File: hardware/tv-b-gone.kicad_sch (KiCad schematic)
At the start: 0 parts

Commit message: Power lines added to KiCad schematic
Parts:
- added C1: 100n, symbol Device:C
- added U1: ATtiny85-20P, Package_DIP:DIP-8_W7.62mm, symbol MCU_Microchip_ATtiny:ATtiny85-20P
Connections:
- new net +5V: C1.2, U1.8 (VCC)
- new net GND: C1.1, U1.4 (GND)

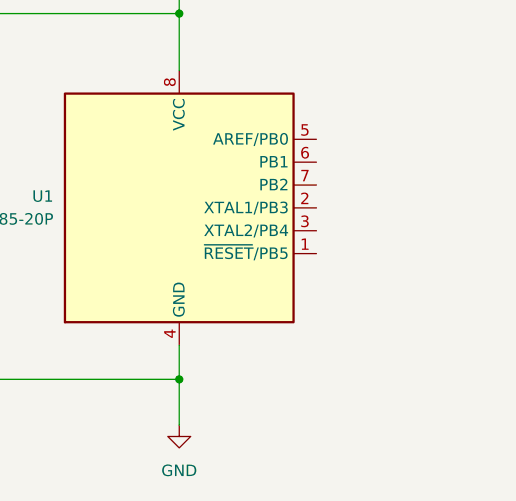
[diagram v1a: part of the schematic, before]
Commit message: added reset circuitry
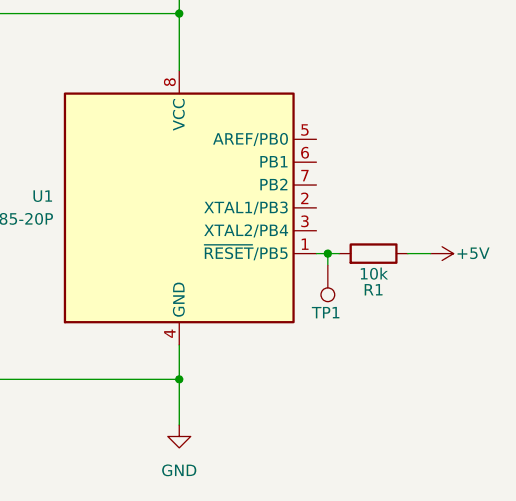
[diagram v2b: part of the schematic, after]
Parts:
- added R1: 10k, Resistor_SMD:R_0805_2012Metric, symbol Device:R
- added TP1: TestPoint, Connector:Tag-Connect_TC2030-IDC-FP_2x03_P1.27mm_Vertical, symbol Connector:TestPoint
- C1: footprint (none) -> Capacitor_SMD:C_0805_2012Metric
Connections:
- net +5V: now also R1.1
- net at U1.1 (~{RESET}/PB5): now also R1.2, TP1.1

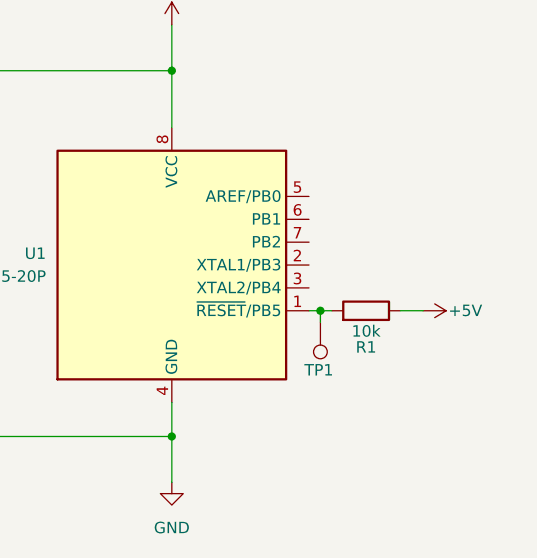
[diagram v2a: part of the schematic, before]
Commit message: ICSP test points added to schematic
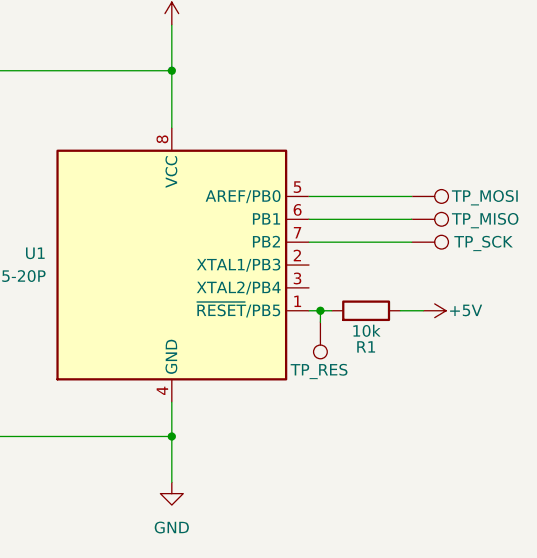
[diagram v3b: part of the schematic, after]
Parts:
- added TP_MISO, TP_MOSI, TP_SCK: TestPoint, TestPoint:TestPoint_Pad_D2.0mm, symbol Connector:TestPoint
- renumbered TP1 to TP_RES
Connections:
- net at U1.5 (AREF/PB0): now also TP_MOSI.1
- net at U1.6 (PB1): now also TP_MISO.1
- net at U1.7 (PB2): now also TP_SCK.1

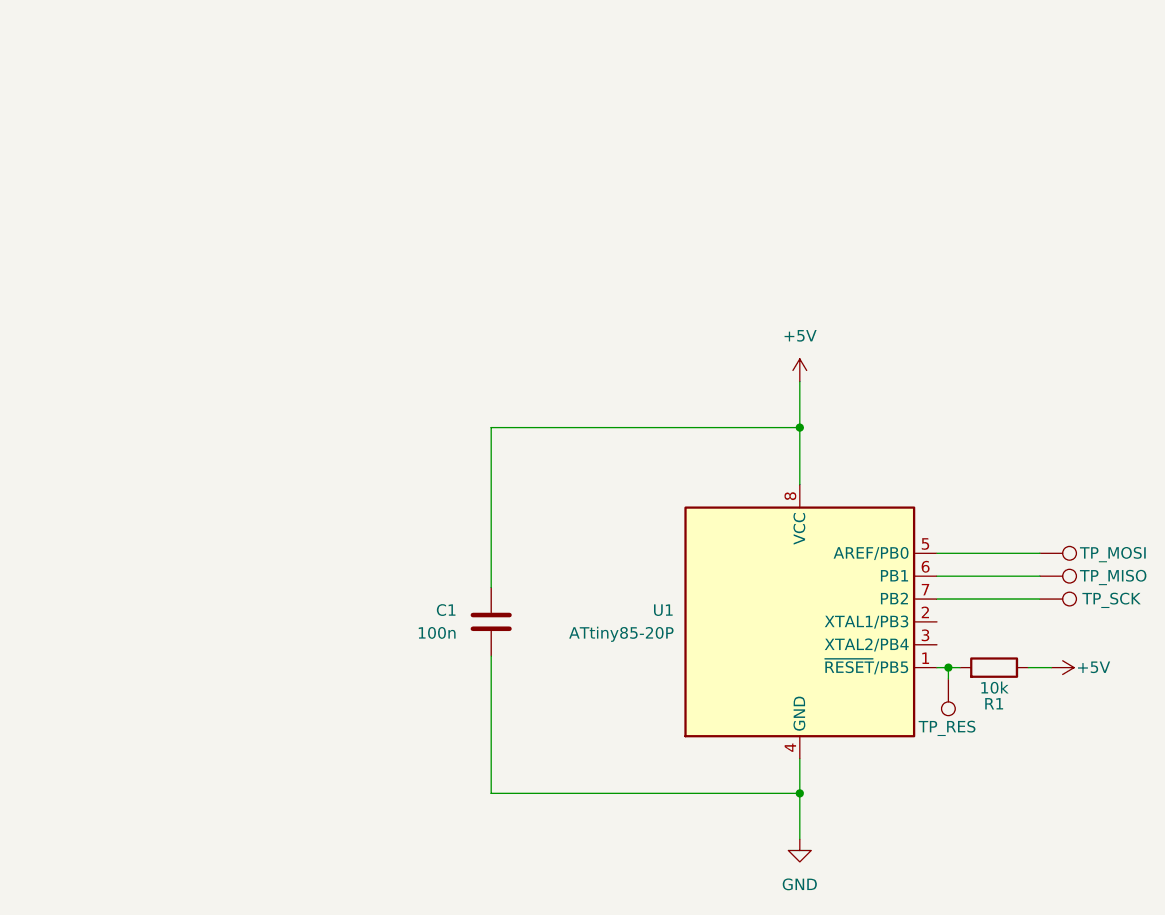
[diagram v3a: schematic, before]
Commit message: Added an IR LED and an N channel MOSFET for controlling it
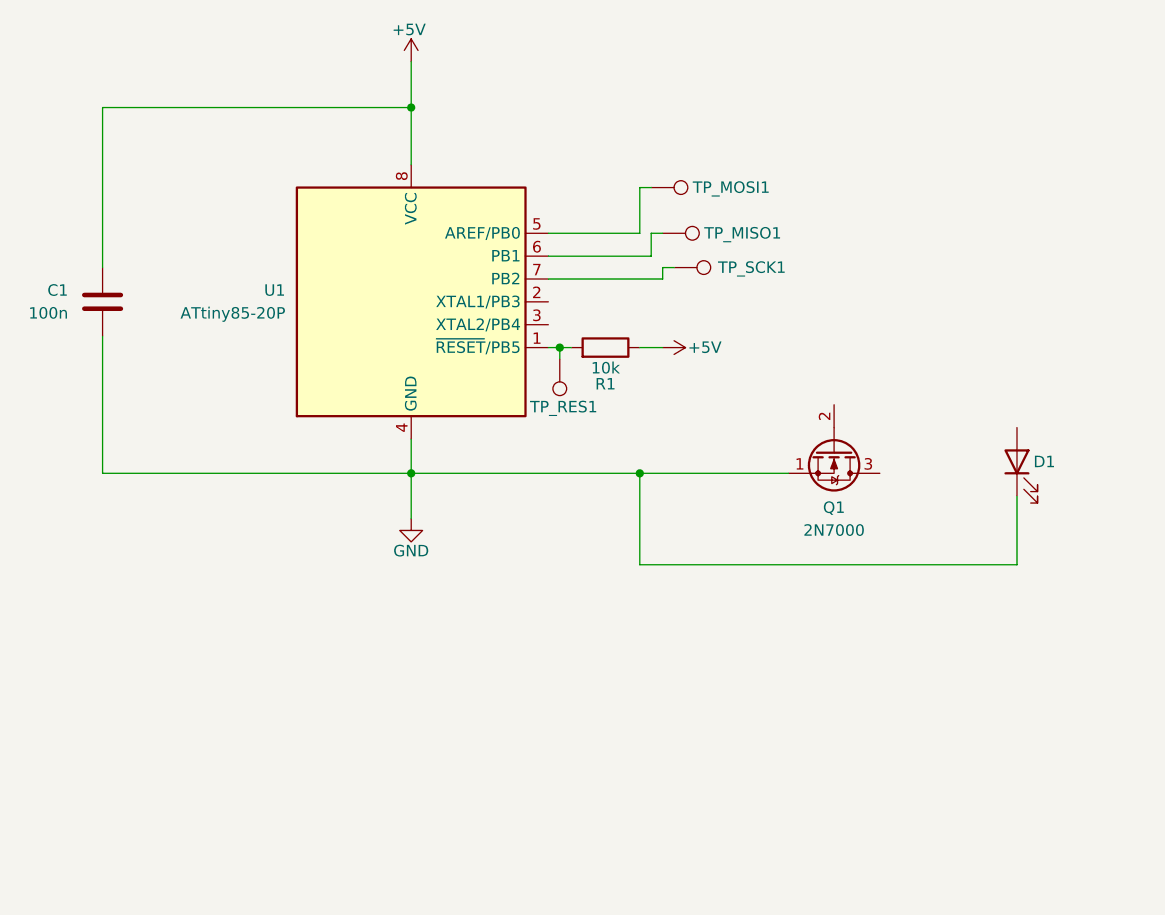
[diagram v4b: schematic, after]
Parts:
- added D1: LED, LED_THT:LED_D5.0mm, symbol Device:LED
- added Q1: 2N7000, Package_TO_SOT_THT:TO-92_Inline, symbol Transistor_FET:2N7000
- TP_RES1: renamed from TP_RES; footprint Connector:Tag-Connect_TC2030-IDC-FP_2x03_P1.27mm_Vertical -> TestPoint:TestPoint_Pad_D2.0mm
- renumbered TP_MISO to TP_MISO1, TP_MOSI to TP_MOSI1, TP_SCK to TP_SCK1
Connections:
- net GND: now also D1.1 (K), Q1.1 (S)
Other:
- title: (none) -> tv-b-gone main PCB
- moved on the sheet: C1, R1, TP_MISO1, TP_MOSI1, TP_RES1, TP_SCK1, U1

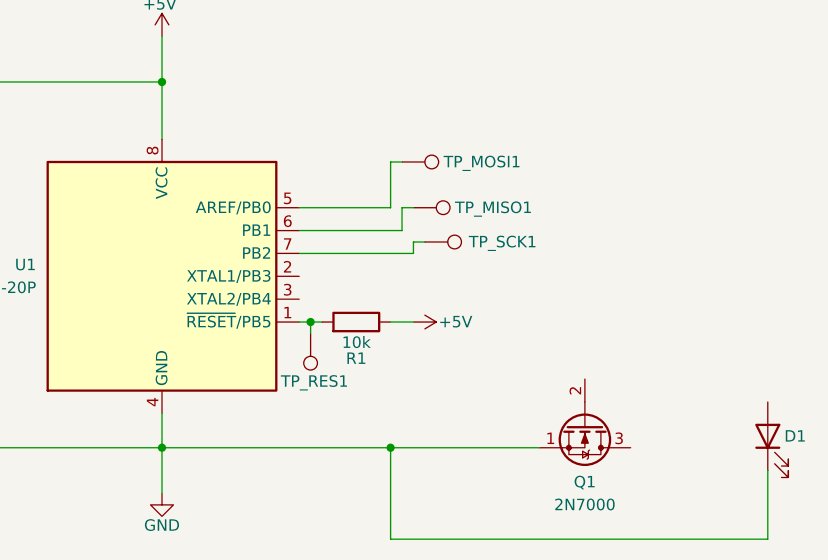
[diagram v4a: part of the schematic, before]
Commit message: Wired the mosfet to the IR LED
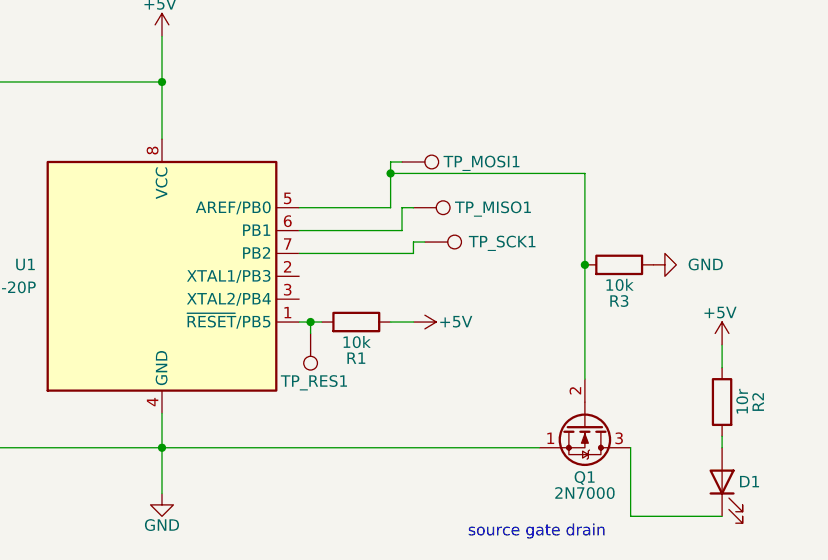
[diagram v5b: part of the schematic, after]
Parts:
- added R2: 10r, Resistor_SMD:R_0805_2012Metric, symbol Device:R
- added R3: 10k, Resistor_SMD:R_0805_2012Metric, symbol Device:R
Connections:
- net +5V: now also R2.1
- net GND: now also R3.1; no longer D1.1 (K)
- net at TP_MOSI1.1, U1.5 (AREF/PB0): now also Q1.2 (G), R3.2
- net at D1.2 (A): now also R2.2
- net at Q1.3 (D): now also D1.1 (K)
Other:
- note added: "source gate drain"
- moved on the sheet: D1

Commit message: Fixed references for ICSP connections
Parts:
- renumbered TP_MISO1 to TP_MISO, TP_MOSI1 to TP_MOSI, TP_RES1 to TP_RESET, TP_SCK1 to TP_SCK
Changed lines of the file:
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@@
 		(in_pos_files yes)
 		(dnp no)
-		(property "Reference" "TP_MOSI1"
+		(property "Reference" "TP_MOSI"
 			(at 114.808 49.53 90)
 			(show_name no)
@@
 			(project "tv-b-gone"
 				(path "/23a371e7-c0c2-4fe5-805f-b61be48edc46"
-					(reference "TP_MOSI1")
+					(reference "TP_MOSI")
 					(unit 1)
 				)
@@
 		(in_pos_files yes)
 		(dnp no)
-		(property "Reference" "TP_RES1"
+		(property "Reference" "TP_RESET"
 			(at 88.138 73.914 0)
 			(show_name no)
@@
 			(project "tv-b-gone"
 				(path "/23a371e7-c0c2-4fe5-805f-b61be48edc46"
-					(reference "TP_RES1")
+					(reference "TP_RESET")
 					(unit 1)
 				)
@@
 		(in_pos_files yes)
 		(dnp no)
-		(property "Reference" "TP_SCK1"
+		(property "Reference" "TP_SCK"
 			(at 116.586 58.42 90)
 			(show_name no)
@@
 			(project "tv-b-gone"
 				(path "/23a371e7-c0c2-4fe5-805f-b61be48edc46"
-					(reference "TP_SCK1")
+					(reference "TP_SCK")
 					(unit 1)
 				)
@@
 		(in_pos_files yes)
 		(dnp no)
-		(property "Reference" "TP_MISO1"
+		(property "Reference" "TP_MISO"
 			(at 116.078 54.61 90)
 			(show_name no)
@@
 			(project "tv-b-gone"
 				(path "/23a371e7-c0c2-4fe5-805f-b61be48edc46"
-					(reference "TP_MISO1")
-					(unit 1)
-				)
+					(reference "TP_MISO")
+					(unit 1)
+				)

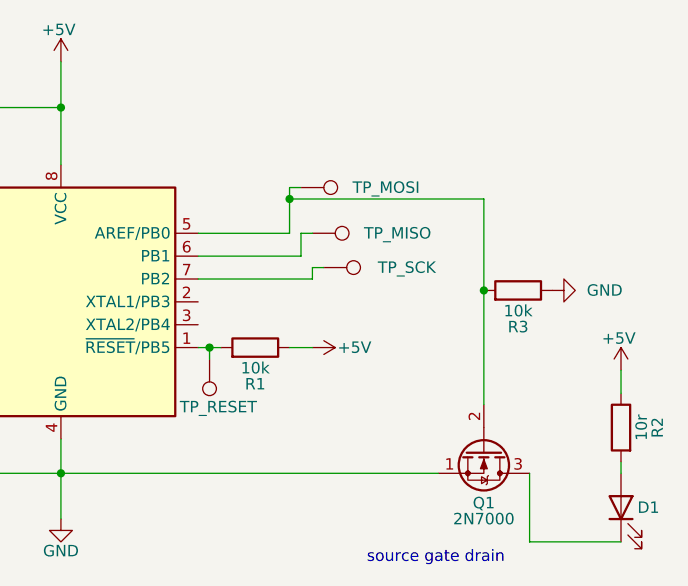
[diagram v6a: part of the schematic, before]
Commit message: Added a tactile switch
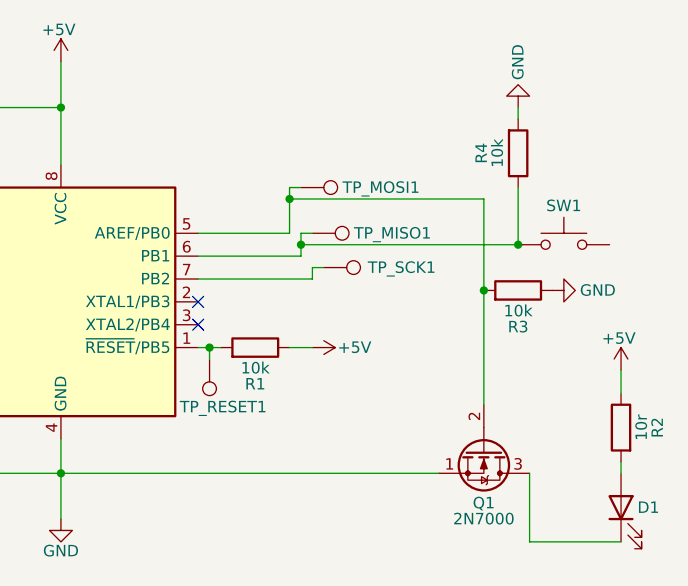
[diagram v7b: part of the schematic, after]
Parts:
- added R4: 10k, Resistor_SMD:R_0805_2012Metric, symbol Device:R
- added SW1: SW_Push, symbol Switch:SW_Push
- renumbered TP_MISO to TP_MISO1, TP_MOSI to TP_MOSI1, TP_RESET to TP_RESET1, TP_SCK to TP_SCK1
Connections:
- net GND: now also R4.2
- net at TP_MISO1.1, U1.6 (PB1): now also R4.1, SW1.1
- no-connect marks 0 -> 2
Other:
- note removed: "source gate drain"

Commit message: Minor fixes
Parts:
- SW1: footprint (none) -> Button_Switch_THT:SW_PUSH_6mm
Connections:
- net +5V: now also SW1.2
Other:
- moved on the sheet: R4
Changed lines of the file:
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@@
+	)
+	(junction
+		(at 124.46 55.88)
+		(diameter 0)
+		(color 0 0 0 0)
 	)
 	(junction
@@
 	)
 	(junction
-		(at 125.73 55.88)
-		(diameter 0)
-		(color 0 0 0 0)
-	)
-	(junction
 		(at 100.33 50.8)
 		(diameter 0)
@@
 	(wire
 		(pts
-			(xy 125.73 49.53) (xy 125.73 55.88)
-		)
-		(stroke
-			(width 0)
-			(type default)
-		)
-	)
-	(wire
-		(pts
 			(xy 40.64 40.64) (xy 74.93 40.64)
 		)
@@
 	(wire
 		(pts
+			(xy 124.46 55.88) (xy 125.73 55.88)
+		)
+		(stroke
+			(width 0)
+			(type default)
+		)
+	)
+	(wire
+		(pts
 			(xy 100.33 54.61) (xy 90.17 54.61)
 		)
@@
 	(wire
 		(pts
-			(xy 101.6 55.88) (xy 125.73 55.88)
+			(xy 101.6 55.88) (xy 124.46 55.88)
 		)
 		(stroke
@@
 	(wire
 		(pts
-			(xy 125.73 40.64) (xy 125.73 41.91)
+			(xy 124.46 40.64) (xy 124.46 41.91)
 		)
 		(stroke
@@
 		(pts
 			(xy 102.87 58.42) (xy 102.87 59.69)
+		)
+		(stroke
+			(width 0)
+			(type default)
+		)
+	)
+	(wire
+		(pts
+			(xy 124.46 49.53) (xy 124.46 55.88)
 		)
 		(stroke
@@
 	(symbol
 		(lib_id "Device:R")
-		(at 125.73 45.72 0)
+		(at 124.46 45.72 0)
 		(mirror x)
 		(unit 1)
@@
 		(dnp no)
 		(property "Reference" "R4"
-			(at 121.666 45.72 90)
+			(at 120.396 45.72 90)
 			(show_name no)
 			(do_not_autoplace no)
@@
 		)
 		(property "Value" "10k"
-			(at 123.444 45.72 90)
+			(at 122.174 45.72 90)
 			(show_name no)
 			(do_not_autoplace no)
@@
 		)
 		(property "Footprint" "Resistor_SMD:R_0805_2012Metric"
-			(at 123.952 45.72 90)
+			(at 122.682 45.72 90)
 			(hide yes)
 			(show_name no)
@@
 		)
 		(property "Datasheet" ""
-			(at 125.73 45.72 0)
+			(at 124.46 45.72 0)
 			(hide yes)
 			(show_name no)
@@
 		)
 		(property "Description" "Resistor"
-			(at 125.73 45.72 0)
+			(at 124.46 45.72 0)
 			(hide yes)
 			(show_name no)
@@
 	(symbol
 		(lib_id "power:GND")
-		(at 125.73 40.64 180)
+		(at 124.46 40.64 180)
 		(unit 1)
 		(body_style 1)
@@
 		(dnp no)
 		(property "Reference" "#PWR06"
-			(at 125.73 34.29 0)
+			(at 124.46 34.29 0)
 			(hide yes)
 			(show_name no)
@@
 		)
 		(property "Value" "GND"
-			(at 125.73 37.592 90)
+			(at 124.46 37.592 90)
 			(show_name no)
 			(do_not_autoplace no)
@@
 		)
 		(property "Footprint" ""
-			(at 125.73 40.64 0)
+			(at 124.46 40.64 0)
 			(hide yes)
 			(show_name no)
@@
 		)
 		(property "Datasheet" ""
-			(at 125.73 40.64 0)
+			(at 124.46 40.64 0)
 			(hide yes)
 			(show_name no)
@@
 		)
 		(property "Description" "Power symbol creates a global label with name \"GND\" , ground"
-			(at 125.73 40.64 0)
+			(at 124.46 40.64 0)
 			(hide yes)
 			(show_name no)
@@
 	)
 	(symbol
+		(lib_id "power:+5V")
+		(at 135.89 55.88 270)
+		(unit 1)
+		(body_style 1)
+		(exclude_from_sim no)
+		(in_bom yes)
+		(on_board yes)
+		(in_pos_files yes)
+		(dnp no)
+		(property "Reference" "#PWR07"
+			(at 132.08 55.88 0)
+			(hide yes)
+			(show_name no)
+			(do_not_autoplace no)
+			(effects
+				(font
+					(size 1.27 1.27)
+				)
+			)
+		)
+		(property "Value" "+5V"
+			(at 139.446 55.626 0)
+			(show_name no)
+			(do_not_autoplace no)
+			(effects
+				(font
+					(size 1.27 1.27)
+				)
+			)
+		)
+		(property "Footprint" ""
+			(at 135.89 55.88 0)
+			(hide yes)
+			(show_name no)
+			(do_not_autoplace no)
+			(effects
+				(font
+					(size 1.27 1.27)
+				)
+			)
+		)
+		(property "Datasheet" ""
+			(at 135.89 55.88 0)
+			(hide yes)
+			(show_name no)
+			(do_not_autoplace no)
+			(effects
+				(font
+					(size 1.27 1.27)
+				)
+			)
+		)
+		(property "Description" "Power symbol creates a global label with name \"+5V\""
+			(at 135.89 55.88 0)
+			(hide yes)
+			(show_name no)
+			(do_not_autoplace no)
+			(effects
+				(font
+					(size 1.27 1.27)
+				)
+			)
+		)
+		(pin "1"
+		)
+		(instances
+			(project "tv-b-gone"
+				(path "/23a371e7-c0c2-4fe5-805f-b61be48edc46"
+					(reference "#PWR07")
+					(unit 1)
+				)
+			)
+		)
+	)
+	(symbol
 		(lib_id "Connector:TestPoint")
 		(at 102.87 54.61 270)
@@
 			)
 		)
-		(property "Footprint" ""
+		(property "Footprint" "Button_Switch_THT:SW_PUSH_6mm"
 			(at 130.81 50.8 0)
 			(hide yes)
